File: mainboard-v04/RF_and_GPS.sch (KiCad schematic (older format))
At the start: 21 parts, among them J11 Conn_01x02, J12 Conn_Coaxial, J5 Conn_Coaxial, J6 Conn_Coaxial, J7 Conn_Coaxial, U10 XTB-40, U11 XTB-40, U12 XTB-40, U13 EP2W+, U14 S1216V8, U15 RFM9xBreakout, U20 RFM9xBreakout, U23 RFM98PW, U24 RFM98PW, U9 XTB-40

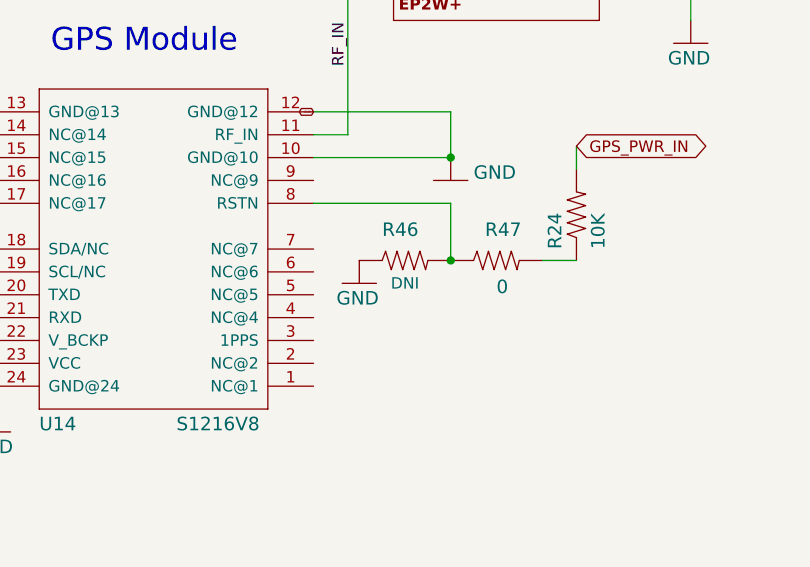
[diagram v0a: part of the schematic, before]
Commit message: adding mainbaordv04 layout and BOM
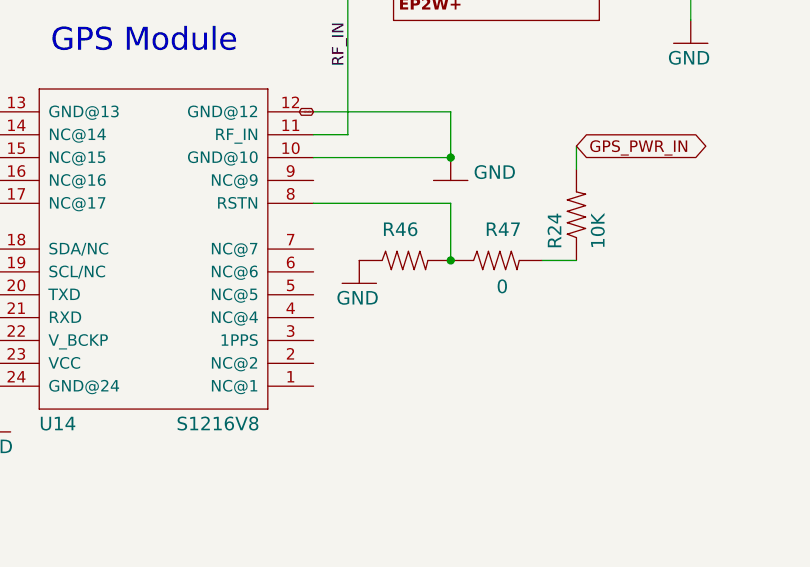
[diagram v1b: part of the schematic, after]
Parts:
- R46: DNI DNI -> (none)
- U10, U11, U12, U14, U9: DNI (none) -> DNI
- U13: DNI (none) -> DNI; Flight (none) -> EP2W+
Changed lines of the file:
@@
 EESchema Schematic File Version 4
-LIBS:mainboard-cache
 EELAYER 30 0
 EELAYER END
@@
 Sheet 3 6
 Title "PyCubed Mainboard"
-Date "2019-11-27"
+Date "2020-01-08"
 Rev "v04"
-Comp "Stanford University"
+Comp ""
 Comment1 "Zac Manchester"
 Comment2 "Max Holliday"
@@
 F 2 "mainboard:S1216_24PIN_PACKAGE" H 8150 5300 50  0001 C CNN
 F 3 "" H 8150 5300 50  0001 C CNN
+F 4 "DNI" H 8150 5300 50  0001 C CNN "DNI"
 	1    8150 5300
 	1    0    0    -1
@@
 F 2 "mainboard:QFN32-5X5MM" H 9700 3700 50  0001 C CNN
 F 3 "" H 9700 3700 50  0001 C CNN
+F 4 "DNI" H 9700 3700 50  0001 C CNN "DNI"
+F 5 "EP2W+" H 9700 3700 50  0001 C CNN "Flight"
 	1    9700 3700
 	1    0    0    -1
@@
 F 2 "custom-footprints:XTB28_MEZ" H 2100 1750 50  0001 C CNN
 F 3 "" H 2100 1750 50  0001 C CNN
+F 4 "DNI" H 2100 1750 50  0001 C CNN "DNI"
 	1    2100 1750
 	1    0    0    -1
@@
 F 2 "custom-footprints:XTB28_MEZ" H 4650 1800 50  0001 C CNN
 F 3 "" H 4650 1800 50  0001 C CNN
+F 4 "DNI" H 4650 1800 50  0001 C CNN "DNI"
 	1    4650 1800
 	1    0    0    -1
@@
 F 2 "custom-footprints:XTB28_MEZ" H 2100 3150 50  0001 C CNN
 F 3 "" H 2100 3150 50  0001 C CNN
+F 4 "DNI" H 2100 3150 50  0001 C CNN "DNI"
 	1    2100 3150
 	1    0    0    -1
@@
 F 2 "custom-footprints:XTB28_MEZ" H 4650 3200 50  0001 C CNN
 F 3 "" H 4650 3200 50  0001 C CNN
+F 4 "DNI" H 4650 3200 50  0001 C CNN "DNI"
 	1    4650 3200
 	1    0    0    -1
@@
 F 2 "Resistor_SMD:R_0603_1608Metric" H 9250 5350 50  0001 C CNN
 F 3 "" H 9250 5350 50  0001 C CNN
-F 4 "DNI" H 9250 5250 50  0000 C CNN "DNI"
+F 4 "" H 9250 5250 50  0000 C CNN "DNI"
 	1    9250 5350
 	1    0    0    -1

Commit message: cleaned up v04
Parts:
- removed R46, R47: 0, Resistor_SMD:R_0603_1608Metric, symbol mainboard:10KOHM-1_10W-1%(0603)0603
- J11, U15, U20, U24: DNI (none) -> DNI
- J12, J5, J6: value Conn_Coaxial -> Amphenol_901-144; DNI (none) -> DNI
- J7: value Conn_Coaxial -> Amphenol_901-144
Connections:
- net at R24.1: now also U14.8 (RSTN)
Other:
- note added: "NOTE: Components labeled "do not install" (DNI) are not populated by default"
- note added: "Optional VCC input for Radio #1\n(if separate than 3V3, DNI R48)"
- note added: "Radio #1"
- note added: "Radio #2"
- note removed: "(if separate than 3V3, DNI R48)"
- note removed: "Radio VCC"
- moved on the sheet: J12, J5, J6, R24, R43, U13, U14, U15, U24
